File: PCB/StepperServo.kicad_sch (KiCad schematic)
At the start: 67 parts, among them P2 Conn_01x04, P3 Conn_01x04, P4 Conn_01x08, U1 AOZ1282CI, U2 A4950E, U4 A4950E, U5 TLE5012B, U7 STM32F103CBTx, U8 LD1117S33CTR, U9 PCA82C251, Y1 Crystal, p7 Conn_01x08

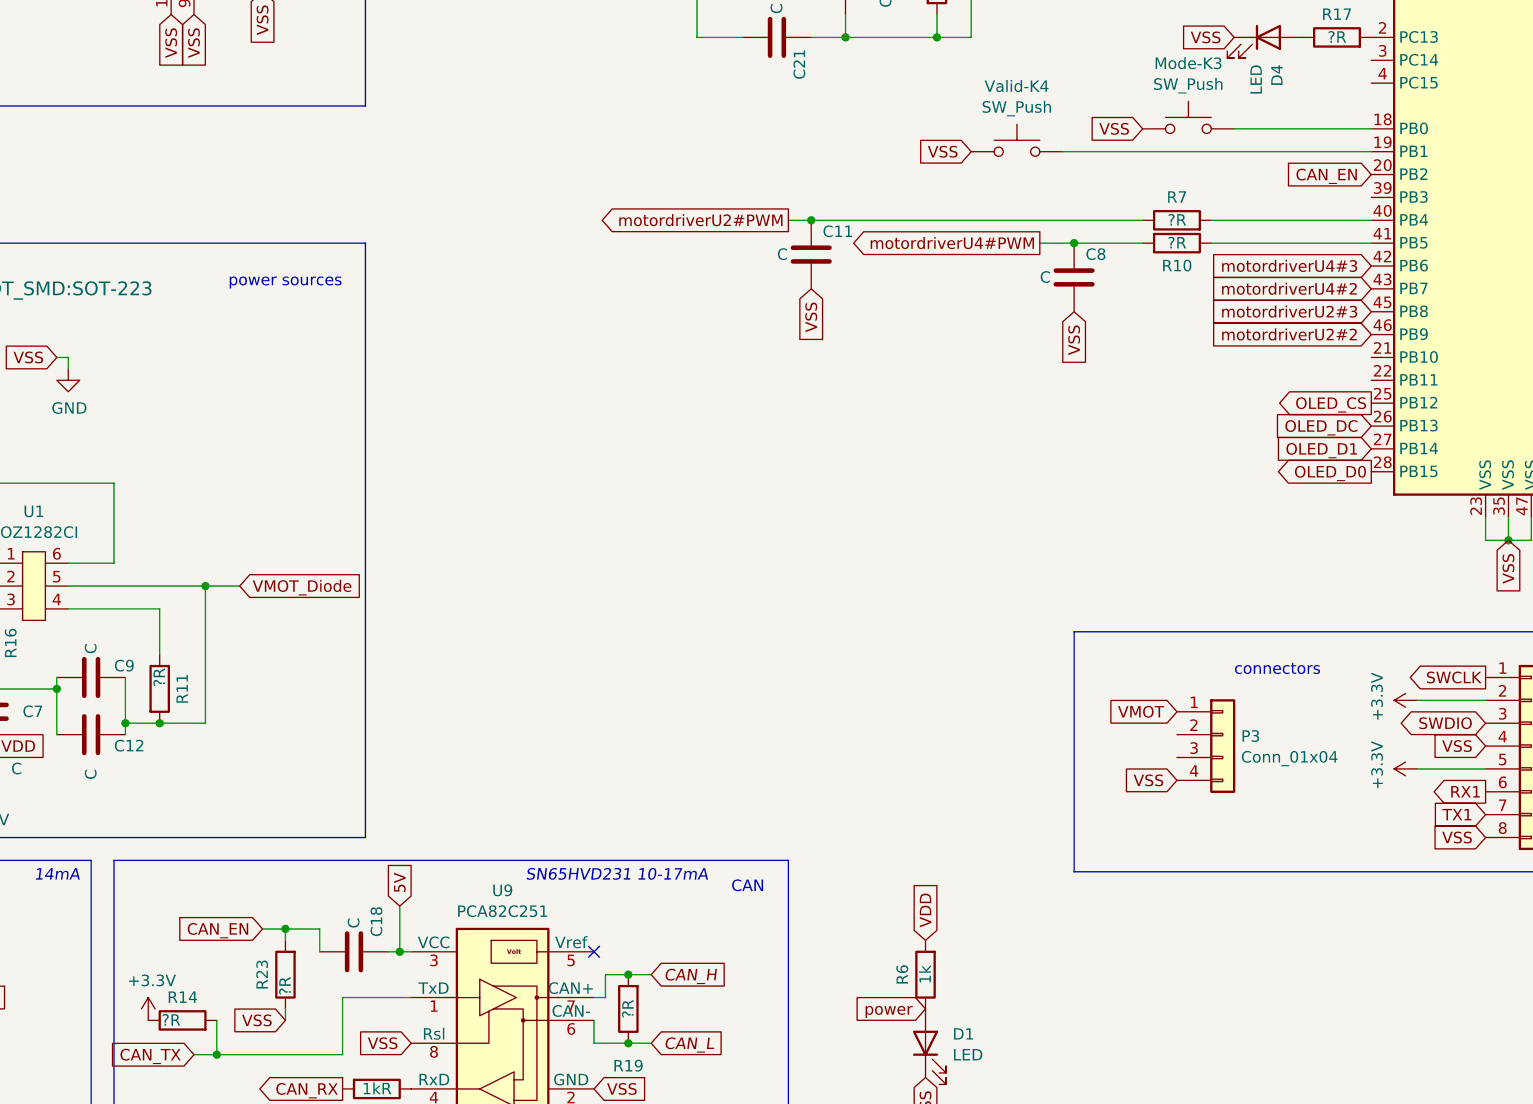
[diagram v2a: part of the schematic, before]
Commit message: Dummy CAN enable line not connected in s42b
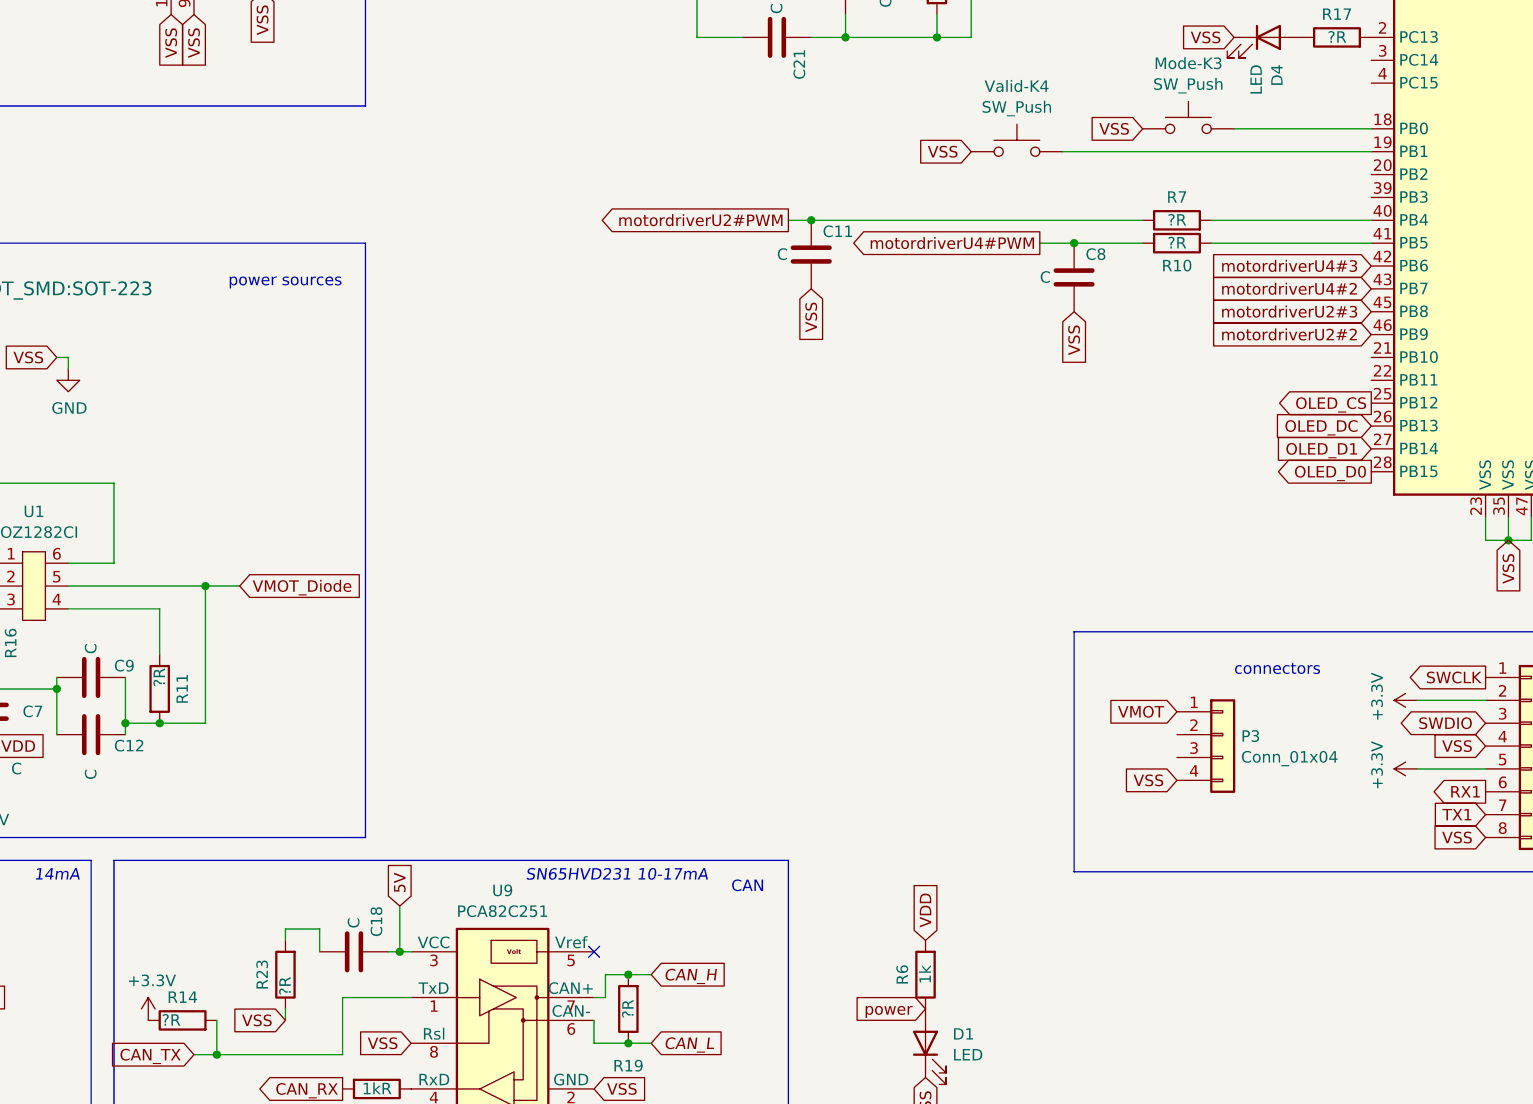
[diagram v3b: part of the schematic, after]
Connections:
- net CAN_EN: no longer names the net of C18.2, R23.2
- net CAN_EN: no longer U7.20 (PB2)
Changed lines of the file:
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@@
   (junction (at 265.43 46.99) (diameter 0) (color 0 0 0 0)
-  )
-  (junction (at 91.44 170.18) (diameter 0) (color 0 0 0 0)
   )
   (junction (at 231.14 46.99) (diameter 0) (color 0 0 0 0)
@@
     (stroke (width 0) (type default) (color 0 0 0 0))
   )
-  (wire (pts (xy 88.9 170.18) (xy 91.44 170.18))
-    (stroke (width 0) (type default) (color 0 0 0 0))
-  )
   (wire (pts (xy 97.79 184.15) (xy 97.79 177.8))
     (stroke (width 0) (type default) (color 0 0 0 0))
@@
     )
   )
-  (global_label "CAN_EN" (shape input) (at 212.09 86.36 180) (fields_autoplaced)
-    (effects (font (size 1.27 1.27)) (justify right))
-    (property "Intersheet References" "${INTERSHEET_REFS}" (id 0) (at 0 0 0)
-      (effects (font (size 1.27 1.27)) hide)
-    )
-  )
   (global_label "TLE_CSQ" (shape input) (at 36.83 182.88 180) (fields_autoplaced)
     (effects (font (size 1.27 1.27)) (justify right))
@@
     (effects (font (size 1.27 1.27)) (justify right))
     (property "Intersheet References" "${INTERSHEET_REFS}" (id 0) (at 0 0 0)
-      (effects (font (size 1.27 1.27)) hide)
-    )
-  )
-  (global_label "CAN_EN" (shape input) (at 88.9 170.18 180) (fields_autoplaced)
-    (effects (font (size 1.27 1.27)) (justify right))
-    (property "Intersheet References" "${INTERSHEET_REFS}" (id 0) (at 0 0 0)

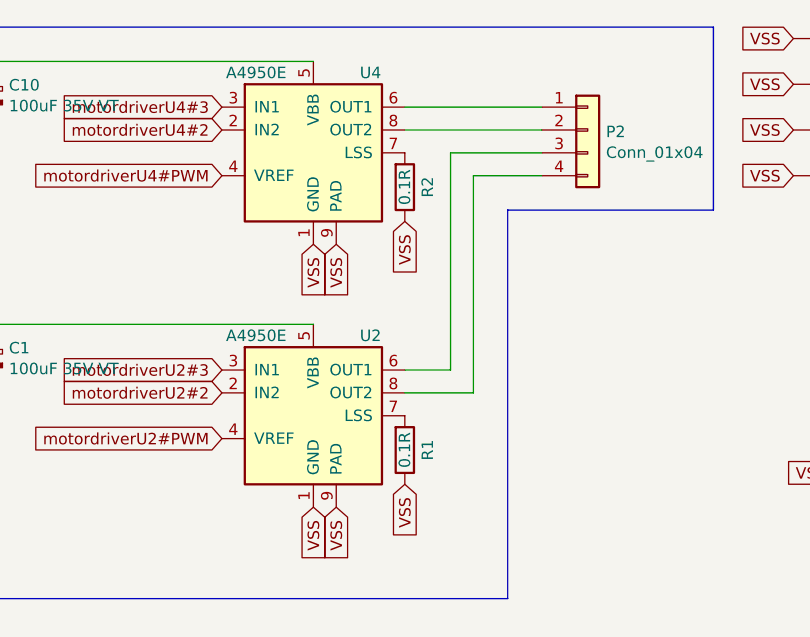
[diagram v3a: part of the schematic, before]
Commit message: S42B has 0.2ohm shunts
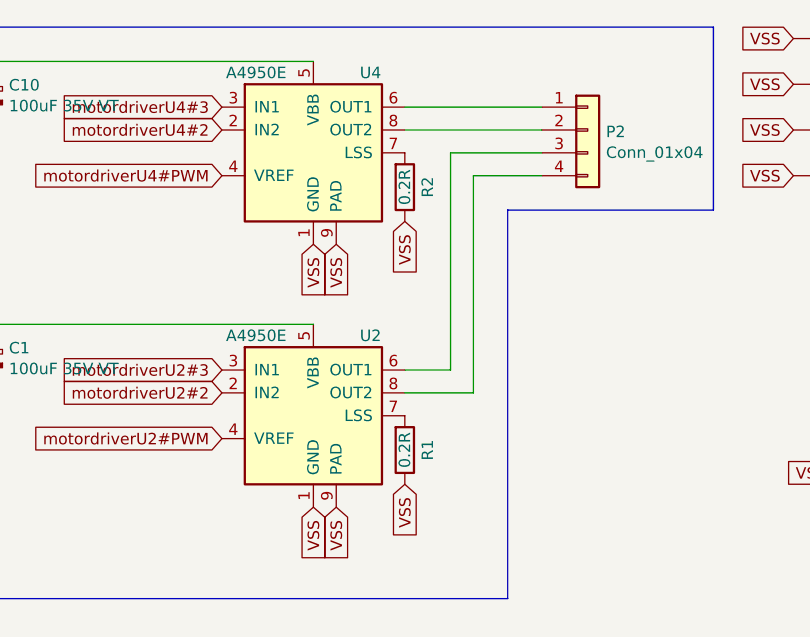
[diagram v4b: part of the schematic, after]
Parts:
- R1, R2: value 0.1R -> 0.2R
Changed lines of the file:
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@@
     (in_bom yes) (on_board yes)
     (property "Reference" "R2" (id 0) (at 91.44 33.02 90))
-    (property "Value" "0.1R" (id 1) (at 88.9 33.02 90))
+    (property "Value" "0.2R" (id 1) (at 88.9 33.02 90))
     (property "Footprint" "Resistor_SMD:R_2512_6332Metric" (id 2) (at 87.122 33.02 90)
       (effects (font (size 1.27 1.27)) hide)
@@
     (in_bom yes) (on_board yes)
     (property "Reference" "R1" (id 0) (at 91.44 62.23 90))
-    (property "Value" "0.1R" (id 1) (at 88.9 62.23 90))
+    (property "Value" "0.2R" (id 1) (at 88.9 62.23 90))
     (property "Footprint" "Resistor_SMD:R_2512_6332Metric" (id 2) (at 87.122 62.23 90)
       (effects (font (size 1.27 1.27)) hide)
@@
     )
     (path "/00000000-0000-0000-0000-000060a5ded0"
-      (reference "R1") (unit 1) (value "0.1R") (footprint "Resistor_SMD:R_2512_6332Metric")
+      (reference "R1") (unit 1) (value "0.2R") (footprint "Resistor_SMD:R_2512_6332Metric")
     )
     (path "/00000000-0000-0000-0000-000060a5d4f4"
-      (reference "R2") (unit 1) (value "0.1R") (footprint "Resistor_SMD:R_2512_6332Metric")
+      (reference "R2") (unit 1) (value "0.2R") (footprint "Resistor_SMD:R_2512_6332Metric")
     )
     (path "/00000000-0000-0000-0000-000060af26da"
